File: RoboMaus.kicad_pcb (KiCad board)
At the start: 4 copper layers, 90 x 95 mm, 111 parts, among them J1 JST, J2 JST, J3 Color_Pins, J4 Gyro_Pins, J5 left_motor_connector, J6 right_motor_connector, J7 USB4145-03-0230-C_REVA2, J8 JTAG, J9 UART, Q1 AO3401A, Q2 2N7002, Q3 2N7002, Q4 2N7002, Q5 2N7002, Q6 2N7002, SW1 SW_DIP_x01, SW2 SW_Enable, SW3 SW_Boot, U1 AMS1117-3.3, U2 L293D, U3 ESP32-S3-MINI-1-N8, U4 USBLC6-2SC6

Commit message: pcb: all wired up, most warnings can't be fixed.
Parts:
- removed C12: 0.1uF, Capacitor_SMD:C_0805_2012Metric_Pad1.18x1.45mm_HandSolder
- removed D10: 1N4148WS, Diode_SMD:D_SOD-323
- removed IR_REC_1, IR_REC_2, IR_REC_3, IR_REC_4, IR_REC_5: TestPoint, TestPoint:TestPoint_THTPad_2.0x2.0mm_Drill1.0mm
- removed J8: JTAG, Connector_PinHeader_2.54mm:PinHeader_1x04_P2.54mm_Vertical
- removed J9: UART, Connector_PinHeader_2.54mm:PinHeader_1x04_P2.54mm_Vertical
- removed Power1: Battery, TestPoint:TestPoint_THTPad_2.0x2.0mm_Drill1.0mm
- removed R31: 5.1k, Resistor_SMD:R_0603_1608Metric_Pad0.98x0.95mm_HandSolder
- removed TP1: 3.3V, TestPoint:TestPoint_THTPad_2.0x2.0mm_Drill1.0mm
- removed TP10: Right_Motor_Pin2, TestPoint:TestPoint_THTPad_2.0x2.0mm_Drill1.0mm
- removed TP11: GPIO1, TestPoint:TestPoint_THTPad_2.0x2.0mm_Drill1.0mm
- removed TP12: GPIO4, TestPoint:TestPoint_THTPad_2.0x2.0mm_Drill1.0mm
- removed TP13: GPIO7, TestPoint:TestPoint_THTPad_2.0x2.0mm_Drill1.0mm
- removed TP14: GPIO10, TestPoint:TestPoint_THTPad_2.0x2.0mm_Drill1.0mm
- removed TP15: GPIO13, TestPoint:TestPoint_THTPad_2.0x2.0mm_Drill1.0mm
- removed TP16: GPIO16, TestPoint:TestPoint_THTPad_2.0x2.0mm_Drill1.0mm
- removed TP17: 5V Usb, TestPoint:TestPoint_THTPad_2.0x2.0mm_Drill1.0mm
- removed TP2: Emitter1, TestPoint:TestPoint_THTPad_2.0x2.0mm_Drill1.0mm
- removed TP3: Emitter2, TestPoint:TestPoint_THTPad_2.0x2.0mm_Drill1.0mm
- removed TP4: Emitter3, TestPoint:TestPoint_THTPad_2.0x2.0mm_Drill1.0mm
- removed TP5: Emitter4, TestPoint:TestPoint_THTPad_2.0x2.0mm_Drill1.0mm
- removed TP6: Emitter5, TestPoint:TestPoint_THTPad_2.0x2.0mm_Drill1.0mm
- removed TP7: Left_Motor_Pin1, TestPoint:TestPoint_THTPad_2.0x2.0mm_Drill1.0mm
- removed TP8: Left_Motor_Pin2, TestPoint:TestPoint_THTPad_2.0x2.0mm_Drill1.0mm
- removed TP9: Right_Motor_Pin1, TestPoint:TestPoint_THTPad_2.0x2.0mm_Drill1.0mm
- added 3.3: Testpoint, TestPoint:TestPoint_THTPad_2.0x2.0mm_Drill1.0mm, F.Cu at (76.1, 30.4)
- added Bat1: Battery, TestPoint:TestPoint_THTPad_2.0x2.0mm_Drill1.0mm, F.Cu at (72.4, 30.4)
- added GPIO1: Testpoint, TestPoint:TestPoint_THTPad_2.0x2.0mm_Drill1.0mm, F.Cu at (75.4, 107.6)
- added GPIO2: Testpoint, TestPoint:TestPoint_THTPad_2.0x2.0mm_Drill1.0mm, F.Cu at (78.8, 107.7)
- added GPIO3: Testpoint, TestPoint:TestPoint_THTPad_2.0x2.0mm_Drill1.0mm, F.Cu at (94.7, 88.8)
- added GPIO4: Testpoint, TestPoint:TestPoint_THTPad_2.0x2.0mm_Drill1.0mm, F.Cu at (88.2, 98.1)
- added GPIO5: Testpoint, TestPoint:TestPoint_THTPad_2.0x2.0mm_Drill1.0mm, F.Cu at (73.7, 82.0)
- added GPIO6: Testpoint, TestPoint:TestPoint_THTPad_2.0x2.0mm_Drill1.0mm, F.Cu at (69.0, 82.1)
- added IRE1: Testpoint, TestPoint:TestPoint_THTPad_2.0x2.0mm_Drill1.0mm, F.Cu at (52.1, 22.7)
- added IRE2: Testpoint, TestPoint:TestPoint_THTPad_2.0x2.0mm_Drill1.0mm, F.Cu at (22.2, 88.7)
- added IRE3: Testpoint, TestPoint:TestPoint_THTPad_2.0x2.0mm_Drill1.0mm, F.Cu at (22.7, 97.8)
- added IRE4: Testpoint, TestPoint:TestPoint_THTPad_2.0x2.0mm_Drill1.0mm, F.Cu at (103.5, 97.8)
- added IRE5: Testpoint, TestPoint:TestPoint_THTPad_2.0x2.0mm_Drill1.0mm, F.Cu at (104.0, 88.5)
- added IRR1: TestPoint, TestPoint:TestPoint_THTPad_2.0x2.0mm_Drill1.0mm, F.Cu at (52.9, 27.3)
- added IRR2: TestPoint, TestPoint:TestPoint_THTPad_2.0x2.0mm_Drill1.0mm, F.Cu at (26.2, 88.8)
- added IRR3: TestPoint, TestPoint:TestPoint_THTPad_2.0x2.0mm_Drill1.0mm, F.Cu at (26.5, 97.8)
- added IRR4: TestPoint, TestPoint:TestPoint_THTPad_2.0x2.0mm_Drill1.0mm, F.Cu at (107.3, 97.8)
- added IRR5: TestPoint, TestPoint:TestPoint_THTPad_2.0x2.0mm_Drill1.0mm, F.Cu at (107.6, 88.5)
- added JTAG1: 2.54MaleDupon, Connector_PinHeader_2.54mm:PinHeader_1x04_P2.54mm_Vertical, F.Cu at (88.9, 79.7)
- added LM1: Testpoint, TestPoint:TestPoint_THTPad_2.0x2.0mm_Drill1.0mm, F.Cu at (47.5, 22.7)
- added LM2: Testpoint, TestPoint:TestPoint_THTPad_2.0x2.0mm_Drill1.0mm, F.Cu at (42.8, 22.8)
- added RM1: Testpoint, TestPoint:TestPoint_THTPad_2.0x2.0mm_Drill1.0mm, F.Cu at (29.1, 22.7)
- added RM2: Testpoint, TestPoint:TestPoint_THTPad_2.0x2.0mm_Drill1.0mm, F.Cu at (37.1, 22.7)
- added UART1: 2.54MaleDupon, Connector_PinHeader_2.54mm:PinHeader_1x04_P2.54mm_Vertical, F.Cu at (81.5, 80.0)
- added USB1: Testpoint, TestPoint:TestPoint_THTPad_2.0x2.0mm_Drill1.0mm, F.Cu at (106.6, 30.8)
- GND1: value GND -> Testpoint
- J1, J2: value JST -> JST-XH
- SW1: value SW_DIP_x01 -> Battery_SW
- U1: footprint Package_TO_SOT_SMD:SOT-223 -> Package_TO_SOT_SMD:SOT-223-3_TabPin2
- U2: footprint Package_DIP:DIP-16_W7.62mm_Socket -> Package_DIP:DIP-16_W7.62mm
- U3: value ESP32-S3-MINI-1-N8 -> ESP32-S3-MINI-1
- moved GND1 212.3 mm to (106.7, 35.8)
- moved C13 203.9 mm to (83.1, 108.0)
- moved R30 202.2 mm to (95.7, 38.4)
- moved SW3 199.4 mm to (83.2, 101.7), turned to 90 degrees
- moved R2 196.6 mm to (91.9, 33.0), turned to 180 degrees
- moved D2 195.9 mm to (92.9, 28.5), turned to 180 degrees
- moved C14 193.5 mm to (91.8, 36.4)
- moved R29 186.5 mm to (67.8, 88.4), turned to 180 degrees
- moved R28 184.3 mm to (64.4, 88.3)
- moved Q1 182.6 mm to (95.9, 32.1)
- moved D1 177.0 mm to (73.4, 44.5)
- moved R1 176.8 mm to (73.4, 41.4)
- moved C1 176.7 mm to (73.3, 33.5), turned to 180 degrees
- moved C2 176.6 mm to (73.2, 36.9), turned to 180 degrees
- moved U4 174.6 mm to (87.2, 35.7)
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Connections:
- C10 pad 1: GND -> Power_To_Load
- C10 pad 2: POWER_TO_LOAD -> GND
- C11 pad 1: POWER_TO_LOAD -> Power_To_Load
- C13 pad 1: GND -> Boot
- C13 pad 2: Boot -> GND
- C14 pad 1: Net-(D10-A) -> 5V_USB
- C8 pad 1: POWER_TO_LOAD -> Power_To_Load
- C9 pad 1: GND -> Power_To_Load
- C9 pad 2: POWER_TO_LOAD -> GND
- D2 pad 1: POWER_TO_LOAD -> Power_To_Load
- J7 pad A4: Net-(D10-A) -> 5V_USB
- J7 pad A9: Net-(D10-A) -> 5V_USB
- J7 pad B4: Net-(D10-A) -> 5V_USB
- J7 pad B5: Net-(J7-CC2) -> Net-(J7-CC1)
- J7 pad B9: Net-(D10-A) -> 5V_USB
- Q1 pad 1: 5V_USB -> Power_To_Load
- Q1 pad 2: Net-(Q1-S) -> 5V_USB
- Q1 pad 3: POWER_TO_LOAD -> Net-(Q1-S)
- SW2 pad 1: Boot -> Enable
- U1 pad 3: POWER_TO_LOAD -> Power_To_Load
- U2 pad 16: POWER_TO_LOAD -> Power_To_Load
- U2 pad 8: POWER_TO_LOAD -> Power_To_Load
- U3 pad 23: USB_D+ -> USB_D-
- U3 pad 24: USB_D- -> USB_D+
- U3 pad 61: (no net) -> GND
- U3 pad 62: (no net) -> GND
- U3 pad 63: (no net) -> GND
- U3 pad 64: (no net) -> GND
- U3 pad 65: (no net) -> GND
- U4 pad 5: Net-(D10-A) -> 5V_USB
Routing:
- net 3.3V: track 0.00 -> 409.3 mm, vias 0 -> 29
- net Receiver1: track 0.00 -> 136.6 mm, vias 0 -> 7
- net Left_Motor_Pin2: track 0.00 -> 134.9 mm, vias 0 -> 7
- net Left_Motor_Pin1: track 0.00 -> 124.8 mm, vias 0 -> 6
- net Emitter1: track 0.00 -> 124.8 mm, vias 0 -> 4
- net Right_Motor_Pin1: track 0.00 -> 113.8 mm, vias 0 -> 6
- net Right_Motor_Pin2: track 0.00 -> 106.9 mm, vias 0 -> 6
- net Power_To_Load: track 0.00 -> 100.7 mm, vias 0 -> 7
- net Receiver2: track 0.00 -> 100.5 mm, vias 0 -> 4
- net TXD0: track 0.00 -> 96.8 mm, vias 0 -> 5
- net USB_D+: track 0.00 -> 87.9 mm, vias 0 -> 4
- net USB_D-: track 0.00 -> 85.9 mm, vias 0 -> 4
- net Color_SDA: track 0.00 -> 81.6 mm, vias 0 -> 3
- net Left_Encoder2: track 0.00 -> 80.9 mm, vias 0 -> 3
- net Emitter2: track 0.00 -> 79.6 mm, vias 0 -> 4
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- added copper zone on B.Cu, net GND
- added copper zone on F.Cu, net GND
- added copper zone on In1.Cu, net GND
- added copper zone on In2.Cu, net GND
- removed copper zone on B.Cu, net (none)
- removed copper zone on F.Cu, net (none)
- removed copper zone on In1.Cu, net (none)
- removed copper zone on In2.Cu, net (none)

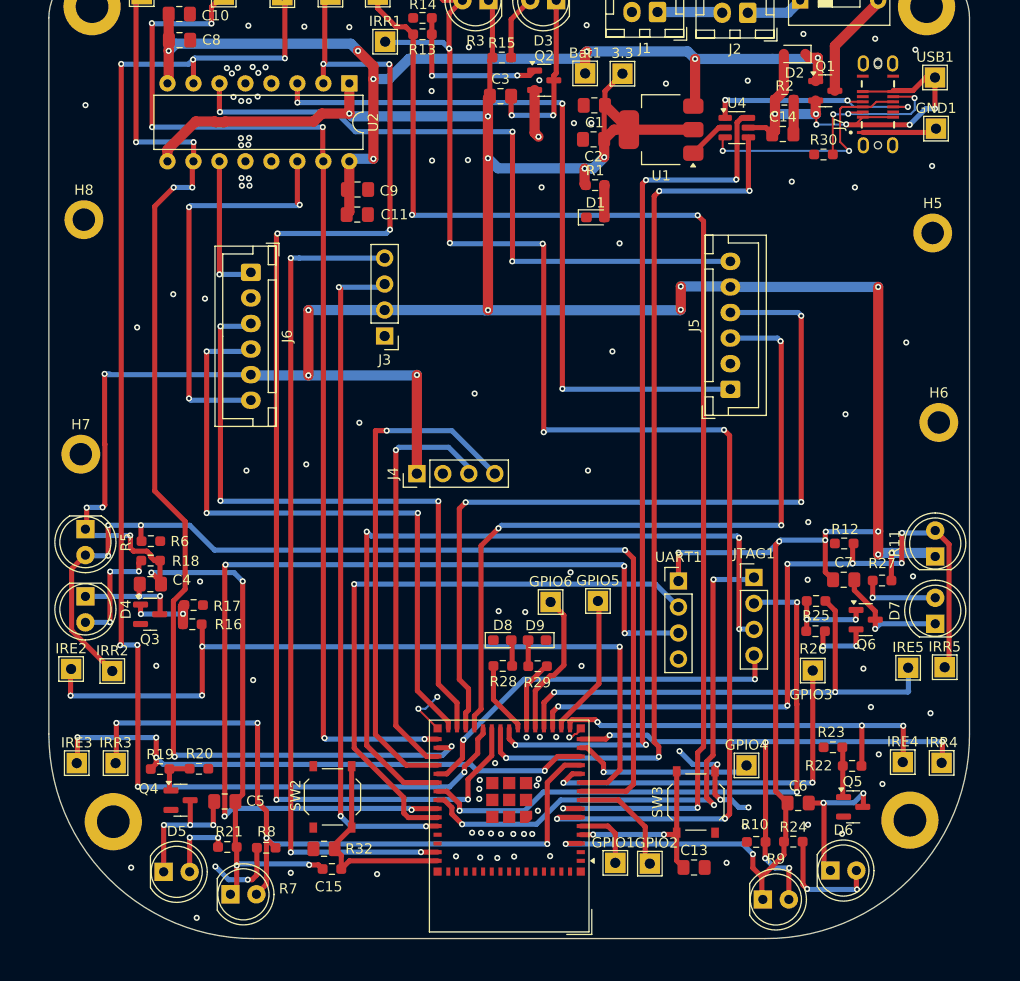
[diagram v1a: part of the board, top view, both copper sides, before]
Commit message: pcb: fixed the wrong mounting holes...
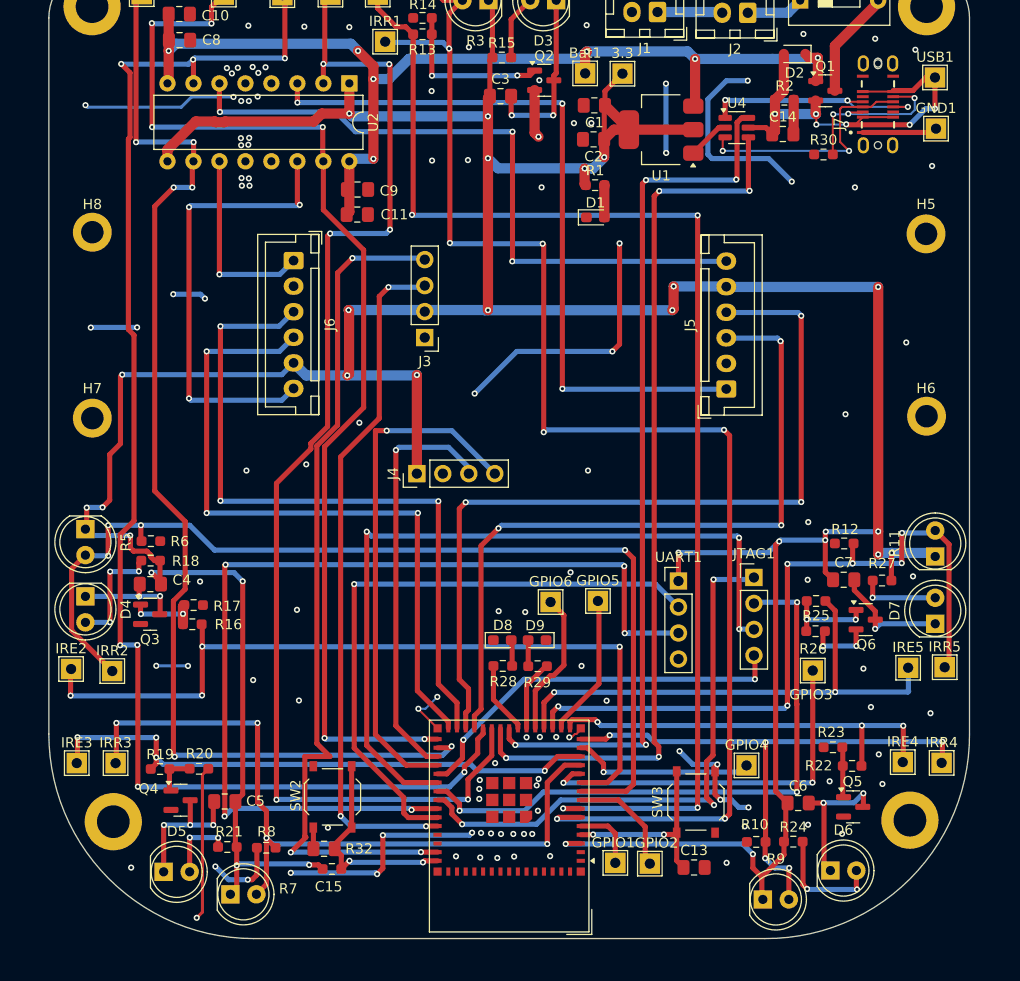
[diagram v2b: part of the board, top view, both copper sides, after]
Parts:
- moved J6 4.33 mm to (43.9, 48.7)
- moved J3 3.93 mm to (56.8, 56.2)
- moved H7 3.70 mm to (24.2, 64.1)
- moved H8 1.62 mm to (24.2, 46.1)
- moved H6 1.32 mm to (105.8, 64.1)
- moved H5 0.66 mm to (105.8, 46.1)
- moved J5 0.40 mm to (86.2, 61.3)
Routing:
- net GND: track 51.4 -> 167.9 mm, vias 108 -> 117
- net Right_Motor_Out1: track 14.2 -> 18.9 mm
- net Right_Encoder2: track 63.2 -> 67.8 mm
- net Right_Encoder1: track 64.4 -> 69.1 mm
- net Right_Motor_Out2: track 40.1 -> 44.7 mm
- net 3.3V: track 409.3 -> 405.0 mm
- net Right_Motor_Pin2: track 106.9 -> 110.1 mm
- net Color_SDA: track 81.6 -> 84.7 mm
- net Left_Motor_Pin1: track 124.8 -> 121.8 mm
- net Left_Motor_Pin2: track 134.9 -> 136.0 mm
- net Color_SCL: track 66.3 -> 67.2 mm
- net Enable: track 20.8 -> 20.9 mm, vias 0 -> 2

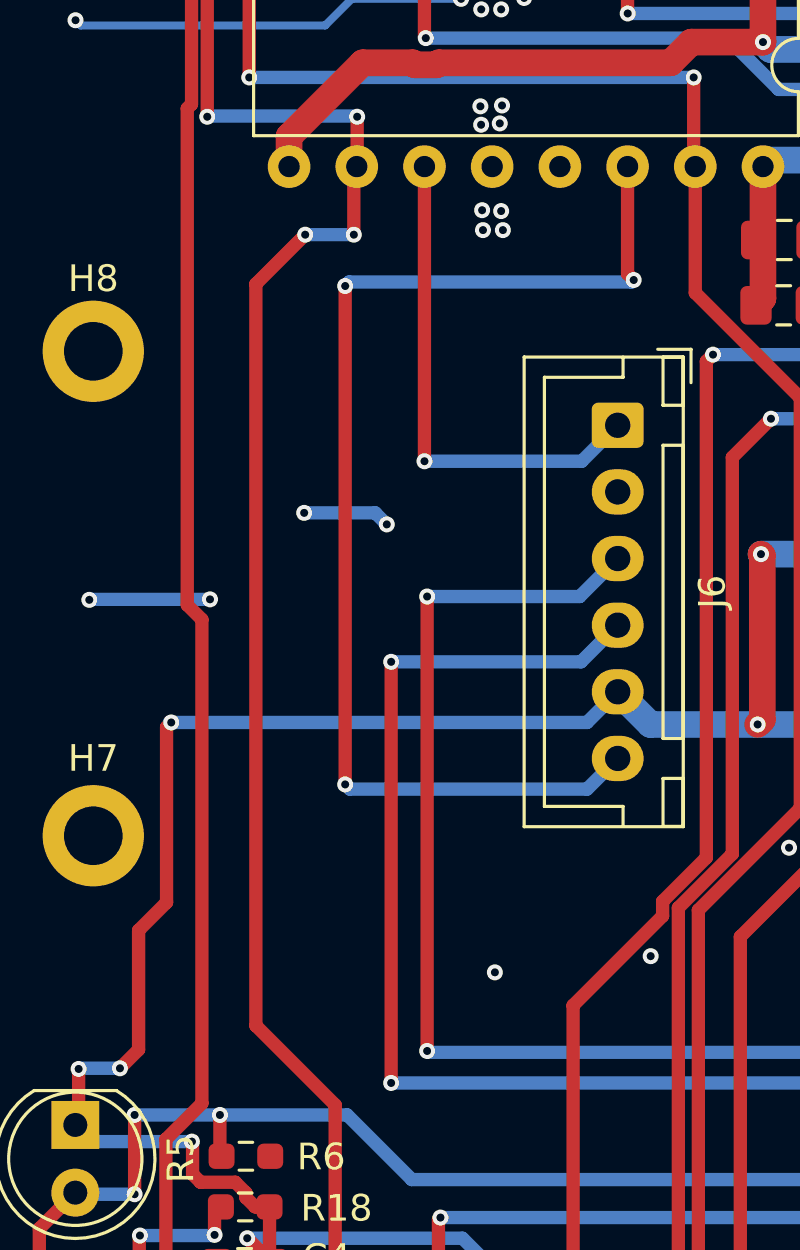
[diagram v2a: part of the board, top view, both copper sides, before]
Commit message: docs: some notes about getting the stencil right
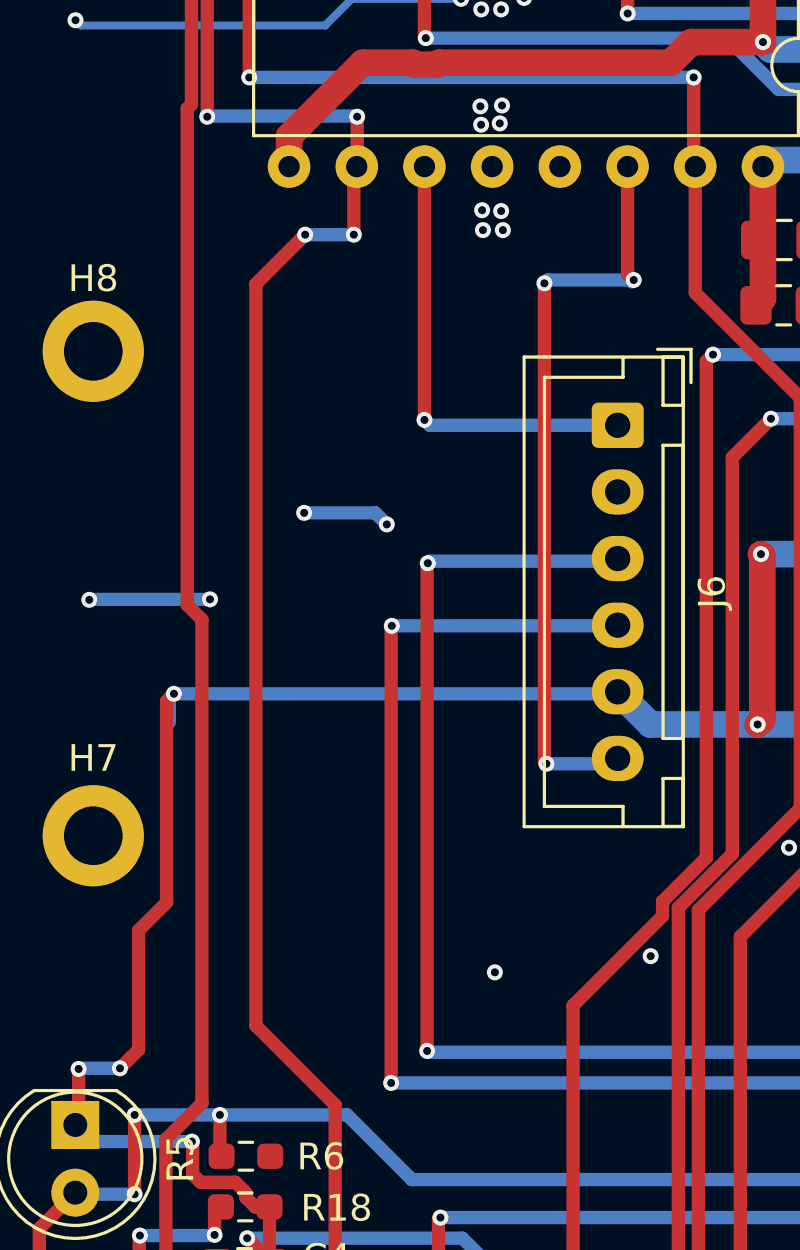
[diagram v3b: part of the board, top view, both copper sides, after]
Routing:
- net Right_Motor_Out2: track 44.7 -> 28.7 mm
- net Right_Motor_Out1: track 18.9 -> 16.8 mm
- net 3.3V: track 405.0 -> 406.6 mm
- net Right_Encoder2: track 67.8 -> 68.6 mm
- net Right_Encoder1: track 69.1 -> 69.8 mm
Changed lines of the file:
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@@
 	)
 	(segment
-		(start 27 60.05)
-		(end 27 66.625)
-		(width 0.5)
-		(layer "F.Cu")
-		(net 1)
-	)
-	(segment
 		(start 88.825 106.75)
 		(end 88.825 108.1)
@@
 	)
 	(segment
+		(start 25.95 72.15)
+		(end 25.25 72.85)
+		(width 0.5)
+		(layer "F.Cu")
+		(net 1)
+	)
+	(segment
 		(start 23.7 74.85)
 		(end 23.575 74.975)
@@
 	)
 	(segment
-		(start 27.175 59.875)
-		(end 27 60.05)
-		(width 0.5)
-		(layer "F.Cu")
-		(net 1)
-	)
-	(segment
 		(start 27.975 76.825)
 		(end 28.275 77.125)
@@
 	)
 	(segment
-		(start 27 66.625)
-		(end 25.95 67.675)
-		(width 0.5)
-		(layer "F.Cu")
-		(net 1)
-	)
-	(segment
 		(start 92.0375 105.35)
 		(end 92.0375 101.925)
@@
 	)
 	(segment
-		(start 25.95 72.15)
-		(end 25.25 72.85)
-		(width 0.5)
-		(layer "F.Cu")
-		(net 1)
-	)
-	(segment
 		(start 76.7 35.8875)
 		(end 74.3625 33.55)
@@
 	)
 	(segment
+		(start 27 66.625)
+		(end 25.95 67.675)
+		(width 0.5)
+		(layer "F.Cu")
+		(net 1)
+	)
+	(segment
 		(start 91.8625 106.8125)
 		(end 89.7 108.975)
@@
 	)
 	(segment
+		(start 27 59.075)
+		(end 27 66.625)
+		(width 0.5)
+		(layer "F.Cu")
+		(net 1)
+	)
+	(segment
 		(start 63.1125 32.65)
 		(end 63.1125 29.125)
@@
 	)
 	(segment
-		(start 25.95 67.675)
-		(end 25.95 72.15)
-		(width 0.5)
-		(layer "F.Cu")
-		(net 1)
-	)
-	(segment
 		(start 74.2875 38.625)
 		(end 74.2875 36.875)
@@
 	)
 	(segment
+		(start 25.95 67.675)
+		(end 25.95 72.15)
+		(width 0.5)
+		(layer "F.Cu")
+		(net 1)
+	)
+	(segment
 		(start 91.05 76.525)
 		(end 91.05 100.5875)
@@
 	)
 	(segment
+		(start 27.275 58.8)
+		(end 27 59.075)
+		(width 0.5)
+		(layer "F.Cu")
+		(net 1)
+	)
+	(segment
 		(start 30.325 78.05)
 		(end 30.8625 78.05)
@@
 	)
 	(via
-		(at 27.175 59.875)
+		(at 27.275 58.8)
 		(size 0.6)
 		(drill 0.3)
@@
 	)
 	(segment
-		(start 42.775 59.875)
-		(end 43.925 58.725)
-		(width 0.5)
-		(layer "B.Cu")
-		(net 1)
-	)
-	(segment
 		(start 49.375 34.35)
 		(end 49.65 34.625)
@@
 	)
 	(segment
-		(start 27.175 59.875)
-		(end 42.775 59.875)
-		(width 0.5)
-		(layer "B.Cu")
-		(net 1)
-	)
-	(segment
 		(start 86.2 51.25)
 		(end 86.225 51.275)
@@
 	)
 	(segment
+		(start 27.1 58.975)
+		(end 27.1 59.875)
+		(width 0.5)
+		(layer "B.Cu")
+		(net 1)
+	)
+	(segment
 		(start 81.55 77.275)
 		(end 90.3 77.275)
@@
 	)
 	(segment
+		(start 27.275 58.8)
+		(end 27.1 58.975)
+		(width 0.5)
+		(layer "B.Cu")
+		(net 1)
+	)
+	(segment
 		(start 49.3 53.56)
 		(end 56.6 53.56)
@@
 	)
 	(segment
+		(start 43.85 58.8)
+		(end 43.925 58.725)
+		(width 0.5)
+		(layer "B.Cu")
+		(net 1)
+	)
+	(segment
 		(start 95.9 76.05)
 		(end 91.525 76.05)
@@
 	)
 	(segment
-		(start 27.1 59.875)
-		(end 27.175 59.875)
-		(width 0.5)
-		(layer "B.Cu")
-		(net 1)
-	)
-	(segment
 		(start 101.225 77.3)
 		(end 102.375 77.3)
@@
 	)
 	(segment
+		(start 27.275 58.8)
+		(end 43.85 58.8)
+		(width 0.5)
+		(layer "B.Cu")
+		(net 1)
+	)
+	(segment
 		(start 73.1875 39.725)
 		(end 74.2875 38.625)
@@
 	(segment
 		(start 36.675 39.02)
-		(end 36.675 50.075)
+		(end 36.675 48.525)
 		(width 0.5)
 		(layer "F.Cu")
@@
 	)
 	(via
-		(at 36.675 50.075)
+		(at 36.675 48.525)
 		(size 0.6)
 		(drill 0.3)
@@
 	)
 	(segment
-		(start 36.675 50.075)
-		(end 42.575 50.075)
+		(start 36.875 48.725)
+		(end 43.925 48.725)
 		(width 0.5)
 		(layer "B.Cu")
@@
 	)
 	(segment
-		(start 42.575 50.075)
-		(end 43.925 48.725)
+		(start 36.675 48.525)
+		(end 36.875 48.725)
 		(width 0.5)
 		(layer "B.Cu")
@@
 	)
 	(segment
-		(start 35.425 73.4)
-		(end 35.425 57.6)
+		(start 59.05 93.8)
+		(end 59.05 94.45)
 		(width 0.5)
 		(layer "F.Cu")
@@
 	)
 	(segment
-		(start 59.05 93.8)
-		(end 59.05 94.45)
+		(start 35.425 56.275)
+		(end 35.45 56.25)
 		(width 0.5)
 		(layer "F.Cu")
@@
 	)
 	(segment
+		(start 35.425 73.4)
+		(end 35.425 56.275)
+		(width 0.5)
+		(layer "F.Cu")
+		(net 32)
+	)
+	(segment
 		(start 56.025 90.775)
 		(end 59.05 93.8)
@@
 	)
 	(via
-		(at 35.425 57.6)
+		(at 35.45 56.25)
 		(size 0.6)
 		(drill 0.3)
@@
 	)
 	(segment
-		(start 35.425 57.6)
-		(end 42.55 57.6)
+		(start 43.9 56.25)
+		(end 43.925 56.225)
 		(width 0.5)
 		(layer "B.Cu")
@@
 	)
 	(segment
-		(start 42.55 57.6)
-		(end 43.925 56.225)
+		(start 35.45 56.25)
+		(end 43.9 56.25)
 		(width 0.5)
 		(layer "B.Cu")
@@
 	)
 	(segment
-		(start 36.775 72.2)
-		(end 36.775 55.15)
+		(start 59.9 91.95)
+		(end 59.9 94.45)
 		(width 0.5)
 		(layer "F.Cu")
@@
 	)
 	(segment
-		(start 59.9 91.95)
-		(end 59.9 94.45)
+		(start 58.075 72.25)
+		(end 58.075 90.125)
 		(width 0.5)
 		(layer "F.Cu")
@@
 	)
 	(segment
-		(start 58.075 72.25)
-		(end 58.075 90.125)
+		(start 36.775 72.2)
+		(end 36.775 53.925)
+		(width 0.5)
+		(layer "F.Cu")
+		(net 33)
+	)
+	(segment
+		(start 36.775 53.925)
+		(end 36.8 53.9)
 		(width 0.5)
 		(layer "F.Cu")
@@
 	)
 	(via
-		(at 36.775 55.15)
+		(at 36.8 53.9)
 		(size 0.6)
 		(drill 0.3)
@@
 	)
 	(segment
-		(start 36.775 55.15)
-		(end 42.5 55.15)
+		(start 36.825 72.25)
+		(end 36.775 72.2)
 		(width 0.5)
 		(layer "B.Cu")
@@
 	)
 	(segment
-		(start 42.5 55.15)
+		(start 43.825 53.825)
 		(end 43.925 53.725)
 		(width 0.5)
@@
 	)
 	(segment
-		(start 36.825 72.25)
-		(end 36.775 72.2)
+		(start 36.875 53.825)
+		(end 43.825 53.825)
+		(width 0.5)
+		(layer "B.Cu")
+		(net 33)
+	)
+	(segment
+		(start 36.8 53.9)
+		(end 36.875 53.825)
 		(width 0.5)
 		(layer "B.Cu")
@@
 	)
 	(segment
-		(start 33.7 62.2)
-		(end 33.7 43.5)
+		(start 41.175 61.35)
+		(end 41.25 61.425)
 		(width 0.5)
 		(layer "F.Cu")
@@
 	)
 	(segment
+		(start 41.175 43.4)
+		(end 41.175 61.35)
+		(width 0.5)
+		(layer "F.Cu")
+		(net 34)
+	)
+	(segment
 		(start 44.525 43.275)
 		(end 44.295 43.045)
@@
 	)
 	(via
-		(at 33.7 43.5)
+		(at 41.175 43.4)
 		(size 0.6)
 		(drill 0.3)
@@
 	)
 	(via
-		(at 33.7 62.2)
+		(at 41.25 61.425)
 		(size 0.6)
 		(drill 0.3)
@@
 	)
 	(segment
-		(start 33.875 62.375)
-		(end 42.775 62.375)
-		(width 0.5)
-		(layer "B.Cu")
-		(net 34)
-	)
-	(segment
-		(start 33.7 62.2)
-		(end 33.875 62.375)
+		(start 41.25 61.425)
+		(end 43.725 61.425)
 		(width 0.5)
 		(layer "B.Cu")
@@
 	)
 	(segment
-		(start 33.85 43.35)
-		(end 33.7 43.5)
+		(start 43.725 61.425)
+		(end 43.925 61.225)
 		(width 0.5)
 		(layer "B.Cu")
@@
 	)
 	(segment
-		(start 44.45 43.35)
-		(end 33.85 43.35)
+		(start 44.525 43.275)
+		(end 41.3 43.275)
 		(width 0.5)
 		(layer "B.Cu")
@@
 	)
 	(segment
-		(start 42.775 62.375)
-		(end 43.925 61.225)
+		(start 41.3 43.275)
+		(end 41.175 43.4)
 		(width 0.5)
 		(layer "B.Cu")
